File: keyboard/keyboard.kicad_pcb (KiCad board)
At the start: 2 copper layers, 94 x 68.6 mm, 20 parts, among them J1 Conn_01x22, J10 Conn_01x01, J11 Conn_01x01, J12 Conn_01x01, J13 Conn_01x01, J14 Conn_01x01, J15 Conn_01x01, J16 Conn_01x01, J2 Conn_01x22, J3 Conn_01x01, J4 Conn_01x01, J5 Conn_01x01, J6 Conn_01x01, J7 Conn_01x01, J8 Conn_01x01, J9 Conn_01x01

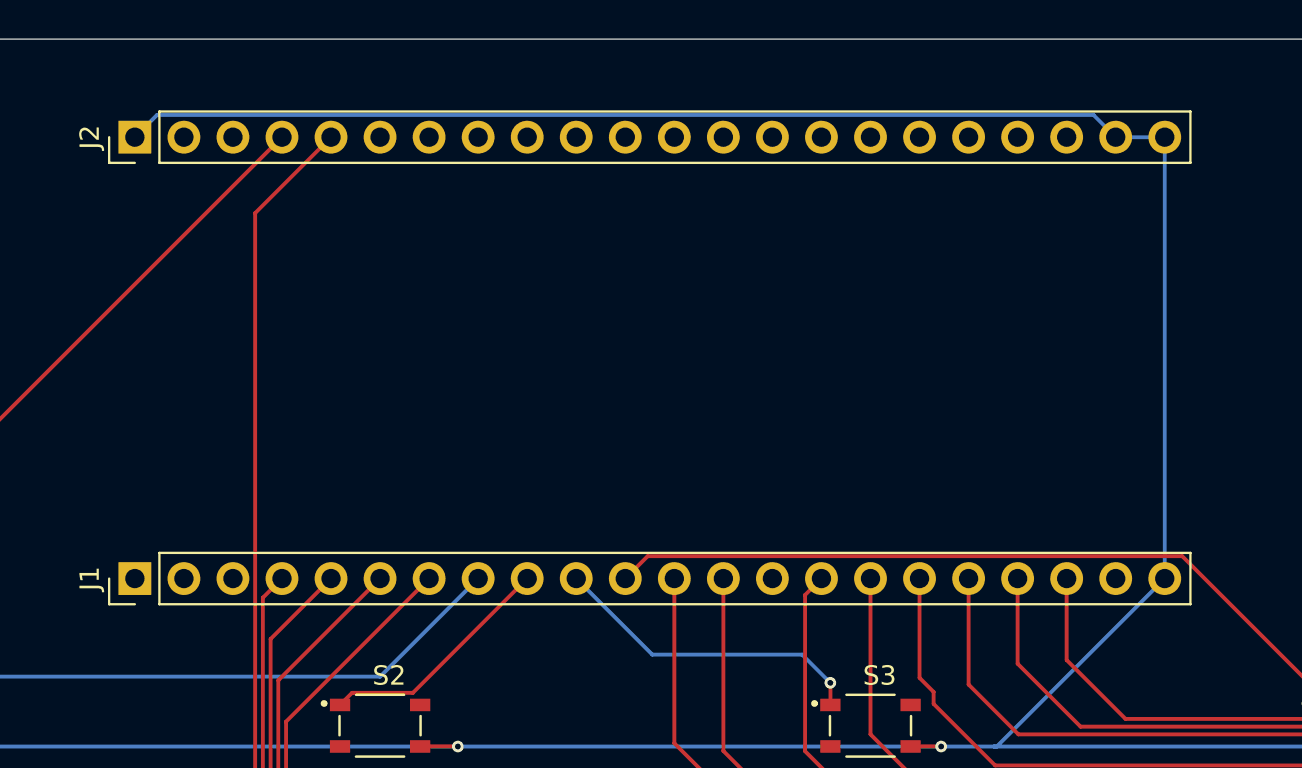
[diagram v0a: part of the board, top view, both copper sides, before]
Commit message: Add silk for ESP32-S3-Devkit-C1
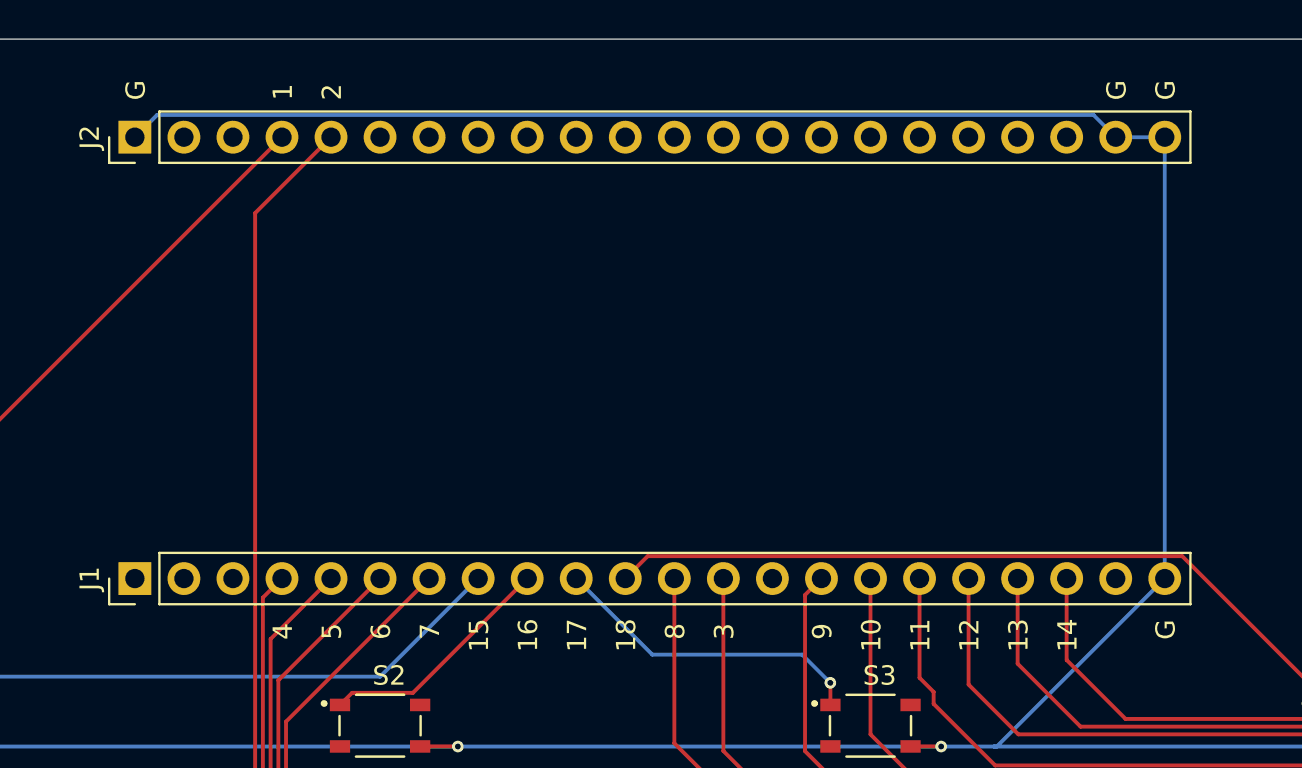
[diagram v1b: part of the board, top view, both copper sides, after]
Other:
- board text added: "1"
- board text added: "10"
- board text added: "11"
- board text added: "12"
- board text added: "13"
- board text added: "14"
- board text added: "15"
- board text added: "16"
- board text added: "17"
- board text added: "18"
- board text added: "2"
- board text added: "3"
- board text added: "4"
- board text added: "5"
- board text added: "6"
- board text added: "7"
- board text added: "8"
- board text added: "9"
- board text added: "G"
